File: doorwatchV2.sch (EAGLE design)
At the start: 29 parts, among them IC2 MAX3232CPE, Q1 IRLZ44Z, T1 BC847, T2 BC847, X1 MKDSN1,5/2-5,08, X2 D-SUB9-H2M09RA

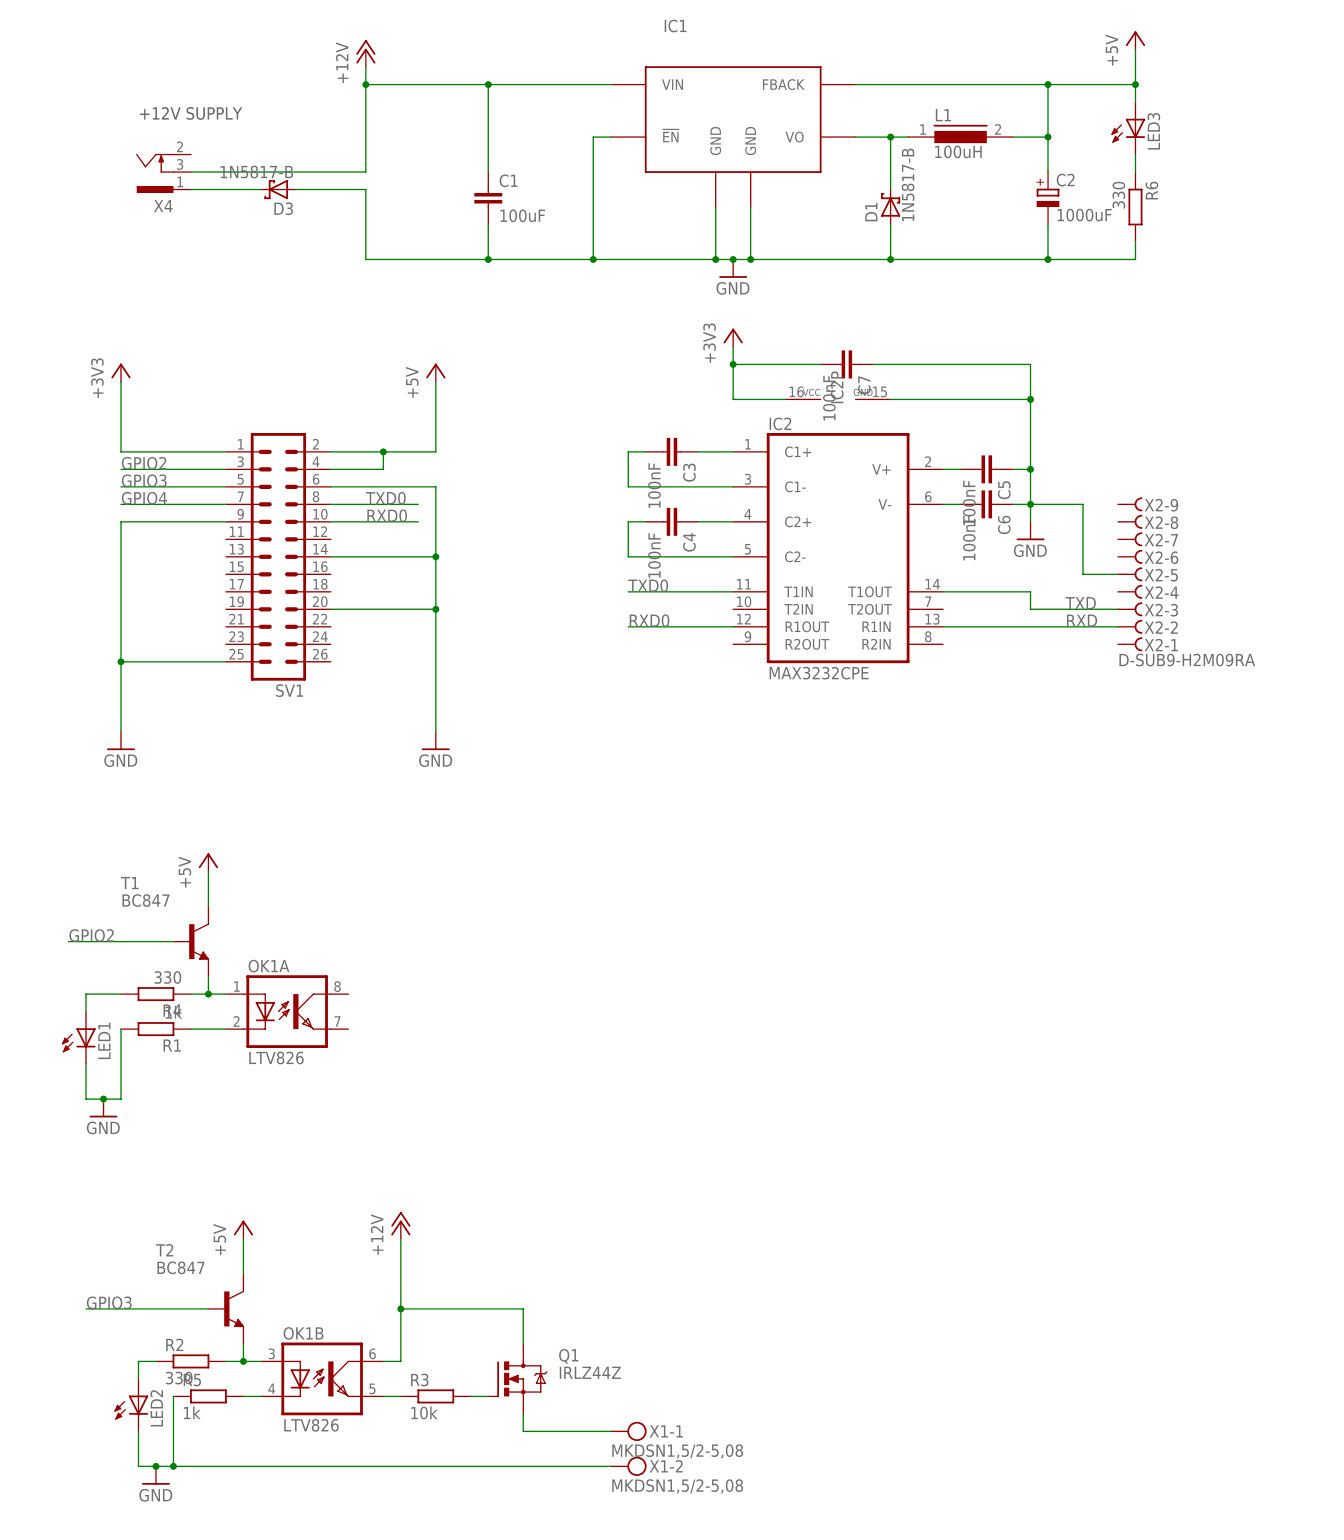
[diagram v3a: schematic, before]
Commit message: added the 230V relay circuit
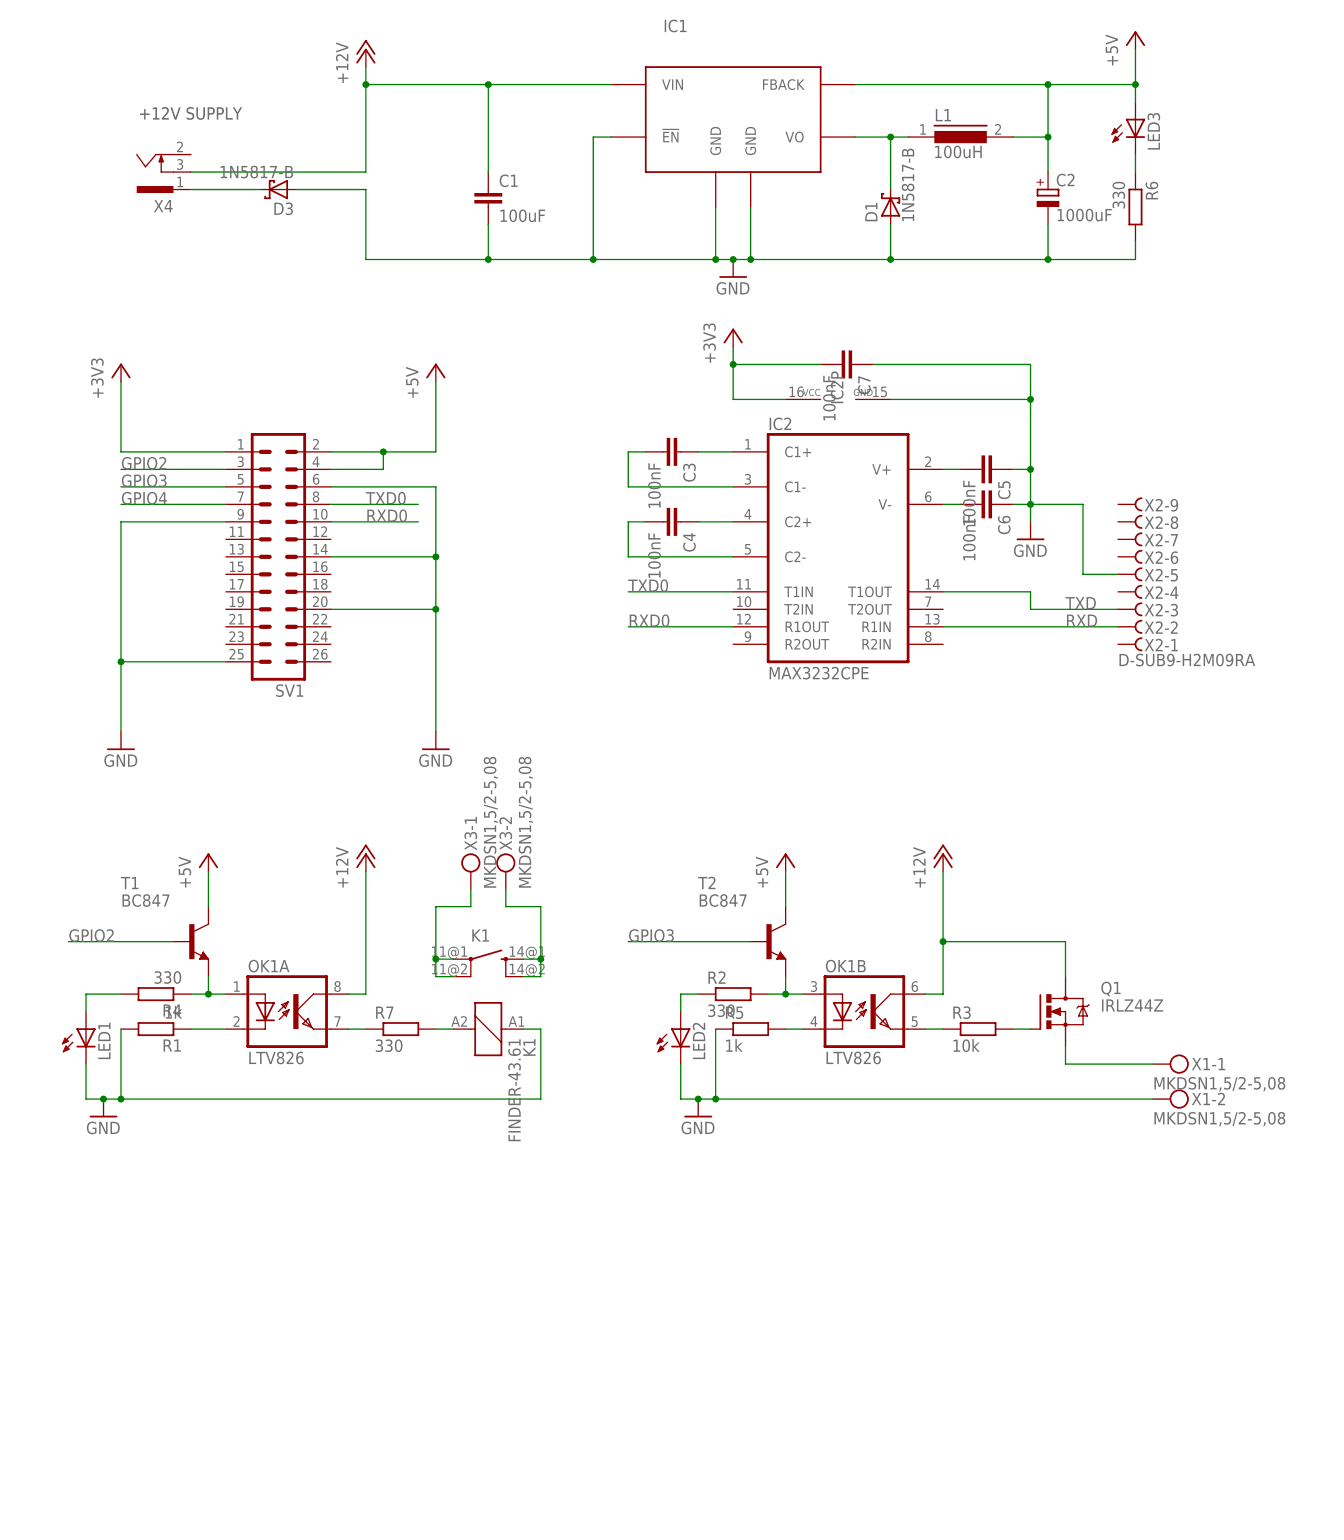
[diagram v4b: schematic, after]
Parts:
- added K1: FINDER-43.61, relay:FINDER-43.61
- added R7: 330, rcl:R-EU_M0805
- added X3: MKDSN1,5/2-5,08, con-phoenix-508:MKDSN1,5/2-5,08
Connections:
- new net N$20: OK1A.EMIT, R7.1
- new net N$21: K1K.2, R7.2
- new net N$22: K1-1.PA, K1-1.PB, X3-1.KL
- new net N$23: K1-1.SA, K1-1.SB, X3-2.KL
- net +12V: now also OK1A.COL
- net GND: now also K1K.1
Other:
- moved on the sheet: LED2, OK1B, Q1, R2, R3, R5, T2, X1-1, X1-2

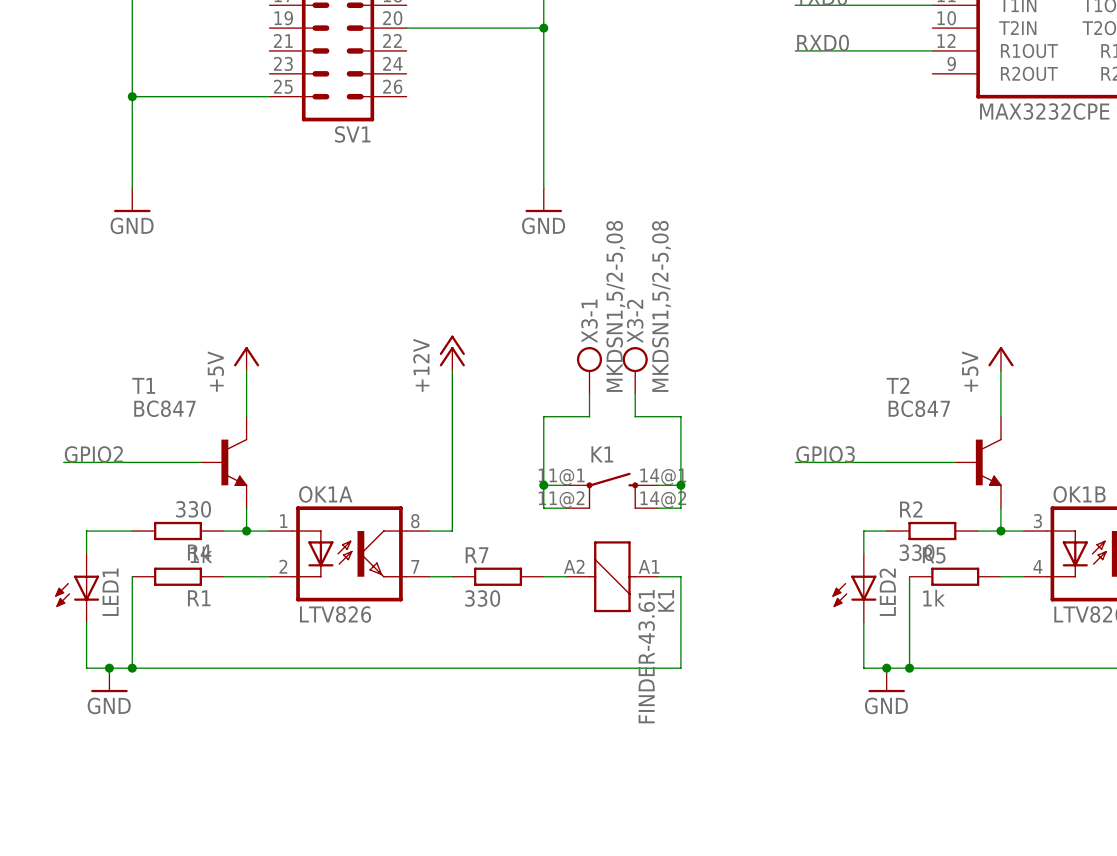
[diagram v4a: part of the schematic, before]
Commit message: fixed bug in relay circuit
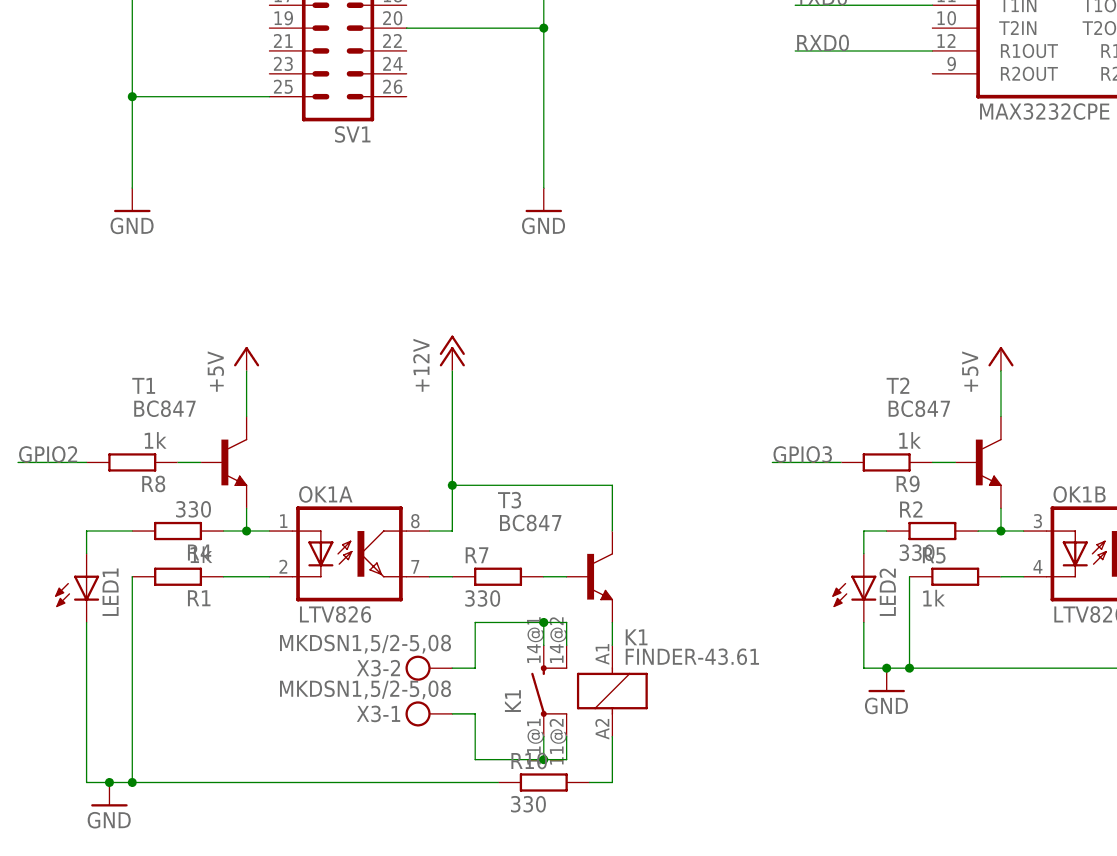
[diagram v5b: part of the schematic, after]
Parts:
- added R10: 330, rcl:R-EU_M0805
- added R8, R9: 1k, rcl:R-EU_M0805
- added T3: BC847, transistor:BC847
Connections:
- new net N$19: R9.1, T2.B
- new net N$24: R8.1, T1.B
- new net N$25: K1K.1, T3.E
- new net N$26: K1K.2, R10.2
- net +12V: now also T3.C
- net GND: now also R10.1; no longer K1K.1
- net GPIO2: now also R8.2; no longer T1.B
- net GPIO3: now also R9.2; no longer T2.B
- net N$21: now also T3.B; no longer K1K.2
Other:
- moved on the sheet: K1, X3-1, X3-2
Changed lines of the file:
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@@
 <part name="P+7" library="supply1" deviceset="+12V" device=""/>
 <part name="X3" library="con-phoenix-508" deviceset="MKDSN1,5/2-5,08" device=""/>
+<part name="R8" library="rcl" deviceset="R-EU_" device="M0805" value="1k"/>
+<part name="R9" library="rcl" deviceset="R-EU_" device="M0805" value="1k"/>
+<part name="T3" library="transistor" deviceset="BC847" device=""/>
+<part name="R10" library="rcl" deviceset="R-EU_" device="M0805" value="330"/>
 </parts>
 <sheets>
@@
 <instance part="R1" gate="G$1" x="-66.04" y="-60.96" rot="R180"/>
 <instance part="R2" gate="G$1" x="17.78" y="-55.88"/>
-<instance part="GND6" gate="1" x="-73.66" y="-73.66"/>
+<instance part="GND6" gate="1" x="-73.66" y="-86.36"/>
 <instance part="LED1" gate="G$1" x="-76.2" y="-60.96"/>
 <instance part="LED2" gate="G$1" x="10.16" y="-60.96"/>
@@
 <instance part="LED3" gate="G$1" x="76.2" y="71.12"/>
 <instance part="R6" gate="G$1" x="76.2" y="58.42" rot="R270"/>
-<instance part="K1" gate="K" x="-17.78" y="-60.96" rot="R270"/>
-<instance part="K1" gate="-1" x="-17.78" y="-50.8" rot="R270"/>
+<instance part="K1" gate="K" x="-17.78" y="-73.66"/>
+<instance part="K1" gate="-1" x="-25.4" y="-73.66"/>
 <instance part="R7" gate="G$1" x="-30.48" y="-60.96"/>
 <instance part="P+7" gate="1" x="-35.56" y="-35.56"/>
-<instance part="X3" gate="-1" x="-20.32" y="-38.1" rot="R90"/>
-<instance part="X3" gate="-2" x="-15.24" y="-38.1" rot="R90"/>
+<instance part="X3" gate="-1" x="-38.1" y="-76.2" rot="R180"/>
+<instance part="X3" gate="-2" x="-38.1" y="-71.12" rot="R180"/>
+<instance part="R8" gate="G$1" x="-71.12" y="-48.26" rot="R180"/>
+<instance part="R9" gate="G$1" x="12.7" y="-48.26" rot="R180"/>
+<instance part="T3" gate="G$1" x="-20.32" y="-60.96"/>
+<instance part="R10" gate="G$1" x="-25.4" y="-83.82"/>
 </instances>
 <busses>
@@
 <segment>
 <pinref part="R1" gate="G$1" pin="2"/>
-<wire x1="-71.12" y1="-60.96" x2="-71.12" y2="-71.12" width="0.1524" layer="91"/>
+<wire x1="-71.12" y1="-60.96" x2="-71.12" y2="-83.82" width="0.1524" layer="91"/>
 <pinref part="LED1" gate="G$1" pin="C"/>
-<wire x1="-76.2" y1="-66.04" x2="-76.2" y2="-71.12" width="0.1524" layer="91"/>
-<wire x1="-76.2" y1="-71.12" x2="-73.66" y2="-71.12" width="0.1524" layer="91"/>
+<wire x1="-76.2" y1="-66.04" x2="-76.2" y2="-83.82" width="0.1524" layer="91"/>
+<wire x1="-76.2" y1="-83.82" x2="-73.66" y2="-83.82" width="0.1524" layer="91"/>
 <pinref part="GND6" gate="1" pin="GND"/>
-<wire x1="-73.66" y1="-71.12" x2="-71.12" y2="-71.12" width="0.1524" layer="91"/>
-<junction x="-73.66" y="-71.12"/>
-<pinref part="K1" gate="K" pin="1"/>
-<wire x1="-12.7" y1="-60.96" x2="-10.16" y2="-60.96" width="0.1524" layer="91"/>
-<wire x1="-10.16" y1="-60.96" x2="-10.16" y2="-71.12" width="0.1524" layer="91"/>
-<wire x1="-10.16" y1="-71.12" x2="-71.12" y2="-71.12" width="0.1524" layer="91"/>
-<junction x="-71.12" y="-71.12"/>
+<wire x1="-73.66" y1="-83.82" x2="-71.12" y2="-83.82" width="0.1524" layer="91"/>
+<junction x="-73.66" y="-83.82"/>
+<pinref part="R10" gate="G$1" pin="1"/>
+<wire x1="-30.48" y1="-83.82" x2="-71.12" y2="-83.82" width="0.1524" layer="91"/>
+<junction x="-71.12" y="-83.82"/>
 </segment>
 <segment>
@@
 </segment>
 <segment>
-<pinref part="T1" gate="G$1" pin="B"/>
-<wire x1="-78.74" y1="-48.26" x2="-63.5" y2="-48.26" width="0.1524" layer="91"/>
-<label x="-78.74" y="-48.26" size="1.778" layer="95"/>
+<pinref part="R8" gate="G$1" pin="2"/>
+<wire x1="-76.2" y1="-48.26" x2="-83.82" y2="-48.26" width="0.1524" layer="91"/>
+<label x="-83.82" y="-48.26" size="1.778" layer="95"/>
 </segment>
 </net>
@@
 </segment>
 <segment>
-<pinref part="T2" gate="G$1" pin="B"/>
-<wire x1="20.32" y1="-48.26" x2="2.54" y2="-48.26" width="0.1524" layer="91"/>
-<label x="2.54" y="-48.26" size="1.778" layer="95"/>
+<pinref part="R9" gate="G$1" pin="2"/>
+<wire x1="7.62" y1="-48.26" x2="0" y2="-48.26" width="0.1524" layer="91"/>
+<label x="0" y="-48.26" size="1.778" layer="95"/>
 </segment>
 </net>
@@
 <pinref part="OK1" gate="A" pin="COL"/>
 <wire x1="-38.1" y1="-55.88" x2="-35.56" y2="-55.88" width="0.1524" layer="91"/>
-<wire x1="-35.56" y1="-55.88" x2="-35.56" y2="-38.1" width="0.1524" layer="91"/>
+<wire x1="-35.56" y1="-55.88" x2="-35.56" y2="-50.8" width="0.1524" layer="91"/>
 <pinref part="P+7" gate="1" pin="+12V"/>
+<pinref part="T3" gate="G$1" pin="C"/>
+<wire x1="-35.56" y1="-50.8" x2="-35.56" y2="-38.1" width="0.1524" layer="91"/>
+<wire x1="-17.78" y1="-55.88" x2="-17.78" y2="-50.8" width="0.1524" layer="91"/>
+<wire x1="-17.78" y1="-50.8" x2="-35.56" y2="-50.8" width="0.1524" layer="91"/>
+<junction x="-35.56" y="-50.8"/>
 </segment>
 </net>
@@
 </segment>
 </net>
+<net name="N$22" class="0">
+<segment>
+<pinref part="K1" gate="-1" pin="PB"/>
+<wire x1="-22.86" y1="-78.74" x2="-22.86" y2="-81.28" width="0.1524" layer="91"/>
+<wire x1="-22.86" y1="-81.28" x2="-25.4" y2="-81.28" width="0.1524" layer="91"/>
+<pinref part="K1" gate="-1" pin="PA"/>
+<wire x1="-25.4" y1="-81.28" x2="-25.4" y2="-78.74" width="0.1524" layer="91"/>
+<wire x1="-25.4" y1="-81.28" x2="-33.02" y2="-81.28" width="0.1524" layer="91"/>
+<wire x1="-33.02" y1="-81.28" x2="-33.02" y2="-76.2" width="0.1524" layer="91"/>
+<junction x="-25.4" y="-81.28"/>
+<pinref part="X3" gate="-1" pin="KL"/>
+<wire x1="-33.02" y1="-76.2" x2="-35.56" y2="-76.2" width="0.1524" layer="91"/>
+</segment>
+</net>
+<net name="N$23" class="0">
+<segment>
+<pinref part="K1" gate="-1" pin="SB"/>
+<wire x1="-22.86" y1="-68.58" x2="-22.86" y2="-66.04" width="0.1524" layer="91"/>
+<wire x1="-22.86" y1="-66.04" x2="-25.4" y2="-66.04" width="0.1524" layer="91"/>
+<pinref part="K1" gate="-1" pin="SA"/>
+<wire x1="-25.4" y1="-66.04" x2="-25.4" y2="-68.58" width="0.1524" layer="91"/>
+<wire x1="-25.4" y1="-66.04" x2="-33.02" y2="-66.04" width="0.1524" layer="91"/>
+<wire x1="-33.02" y1="-66.04" x2="-33.02" y2="-71.12" width="0.1524" layer="91"/>
+<junction x="-25.4" y="-66.04"/>
+<pinref part="X3" gate="-2" pin="KL"/>
+<wire x1="-33.02" y1="-71.12" x2="-35.56" y2="-71.12" width="0.1524" layer="91"/>
+</segment>
+</net>
+<net name="N$19" class="0">
+<segment>
+<pinref part="R9" gate="G$1" pin="1"/>
+<pinref part="T2" gate="G$1" pin="B"/>
+<wire x1="17.78" y1="-48.26" x2="20.32" y2="-48.26" width="0.1524" layer="91"/>
+</segment>
+</net>
+<net name="N$24" class="0">
+<segment>
+<pinref part="R8" gate="G$1" pin="1"/>
+<pinref part="T1" gate="G$1" pin="B"/>
+<wire x1="-66.04" y1="-48.26" x2="-63.5" y2="-48.26" width="0.1524" layer="91"/>
+</segment>
+</net>
 <net name="N$20" class="0">
 <segment>
@@
 <segment>
 <pinref part="R7" gate="G$1" pin="2"/>
+<pinref part="T3" gate="G$1" pin="B"/>
+<wire x1="-25.4" y1="-60.96" x2="-22.86" y2="-60.96" width="0.1524" layer="91"/>
+</segment>
+</net>
+<net name="N$25" class="0">
+<segment>
+<pinref part="T3" gate="G$1" pin="E"/>
+<pinref part="K1" gate="K" pin="1"/>
+<wire x1="-17.78" y1="-66.04" x2="-17.78" y2="-68.58" width="0.1524" layer="91"/>
+</segment>
+</net>
+<net name="N$26" class="0">
+<segment>
 <pinref part="K1" gate="K" pin="2"/>
-<wire x1="-25.4" y1="-60.96" x2="-22.86" y2="-60.96" width="0.1524" layer="91"/>
-</segment>
-</net>
-<net name="N$22" class="0">
-<segment>
-<pinref part="K1" gate="-1" pin="PB"/>
-<wire x1="-22.86" y1="-53.34" x2="-25.4" y2="-53.34" width="0.1524" layer="91"/>
-<wire x1="-25.4" y1="-53.34" x2="-25.4" y2="-50.8" width="0.1524" layer="91"/>
-<pinref part="K1" gate="-1" pin="PA"/>
-<wire x1="-25.4" y1="-50.8" x2="-22.86" y2="-50.8" width="0.1524" layer="91"/>
-<wire x1="-25.4" y1="-50.8" x2="-25.4" y2="-43.18" width="0.1524" layer="91"/>
-<wire x1="-25.4" y1="-43.18" x2="-20.32" y2="-43.18" width="0.1524" layer="91"/>
-<junction x="-25.4" y="-50.8"/>
-<pinref part="X3" gate="-1" pin="KL"/>
-<wire x1="-20.32" y1="-43.18" x2="-20.32" y2="-40.64" width="0.1524" layer="91"/>
-</segment>
-</net>
-<net name="N$23" class="0">
-<segment>
-<pinref part="K1" gate="-1" pin="SB"/>
-<wire x1="-12.7" y1="-53.34" x2="-10.16" y2="-53.34" width="0.1524" layer="91"/>
-<wire x1="-10.16" y1="-53.34" x2="-10.16" y2="-50.8" width="0.1524" layer="91"/>
-<pinref part="K1" gate="-1" pin="SA"/>
-<wire x1="-10.16" y1="-50.8" x2="-12.7" y2="-50.8" width="0.1524" layer="91"/>
-<wire x1="-10.16" y1="-50.8" x2="-10.16" y2="-43.18" width="0.1524" layer="91"/>
-<wire x1="-10.16" y1="-43.18" x2="-15.24" y2="-43.18" width="0.1524" layer="91"/>
-<junction x="-10.16" y="-50.8"/>
-<pinref part="X3" gate="-2" pin="KL"/>
-<wire x1="-15.24" y1="-43.18" x2="-15.24" y2="-40.64" width="0.1524" layer="91"/>
-</segment>
-</net>
+<pinref part="R10" gate="G$1" pin="2"/>
+<wire x1="-17.78" y1="-78.74" x2="-17.78" y2="-83.82" width="0.1524" layer="91"/>
+<wire x1="-17.78" y1="-83.82" x2="-20.32" y2="-83.82" width="0.1524" layer="91"/>
+</segment>
+</net>
